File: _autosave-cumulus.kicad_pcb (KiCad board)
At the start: 2 copper layers, 147.6 x 122.3 mm, 42 parts

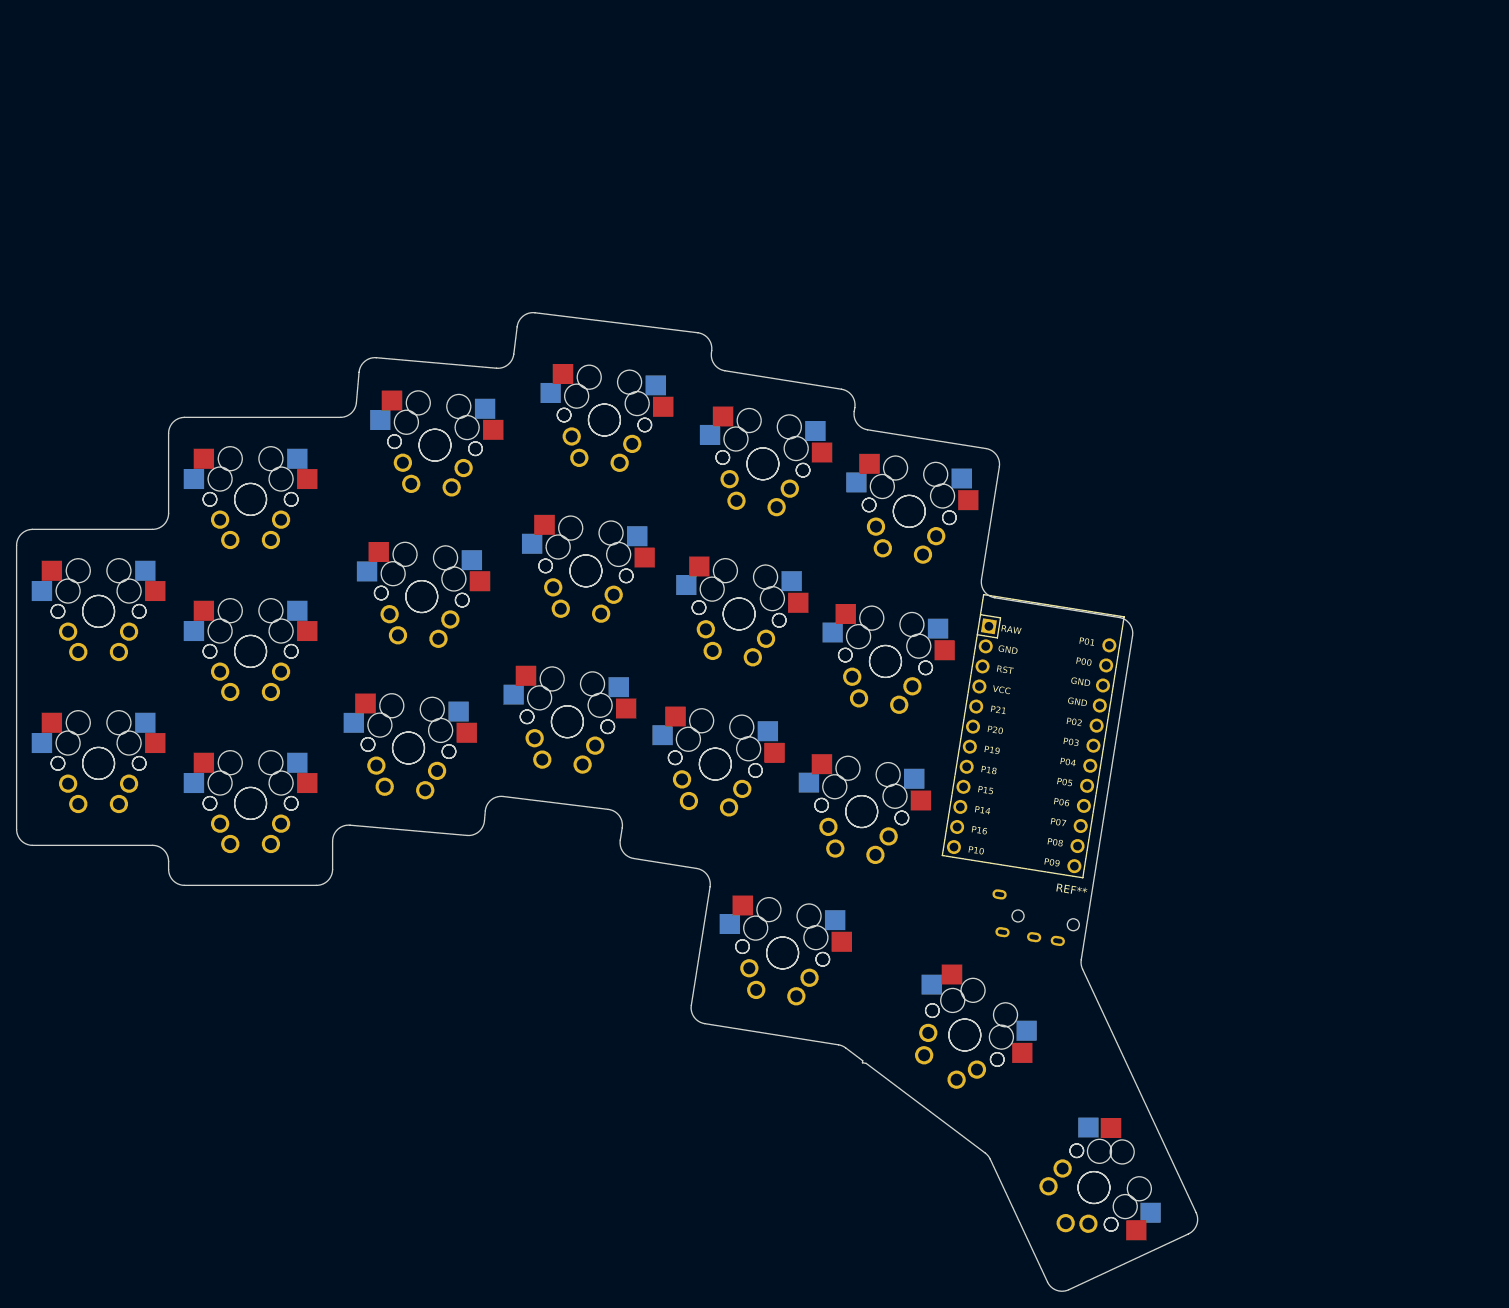
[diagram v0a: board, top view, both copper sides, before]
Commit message: Reversible ProMicro footprint added
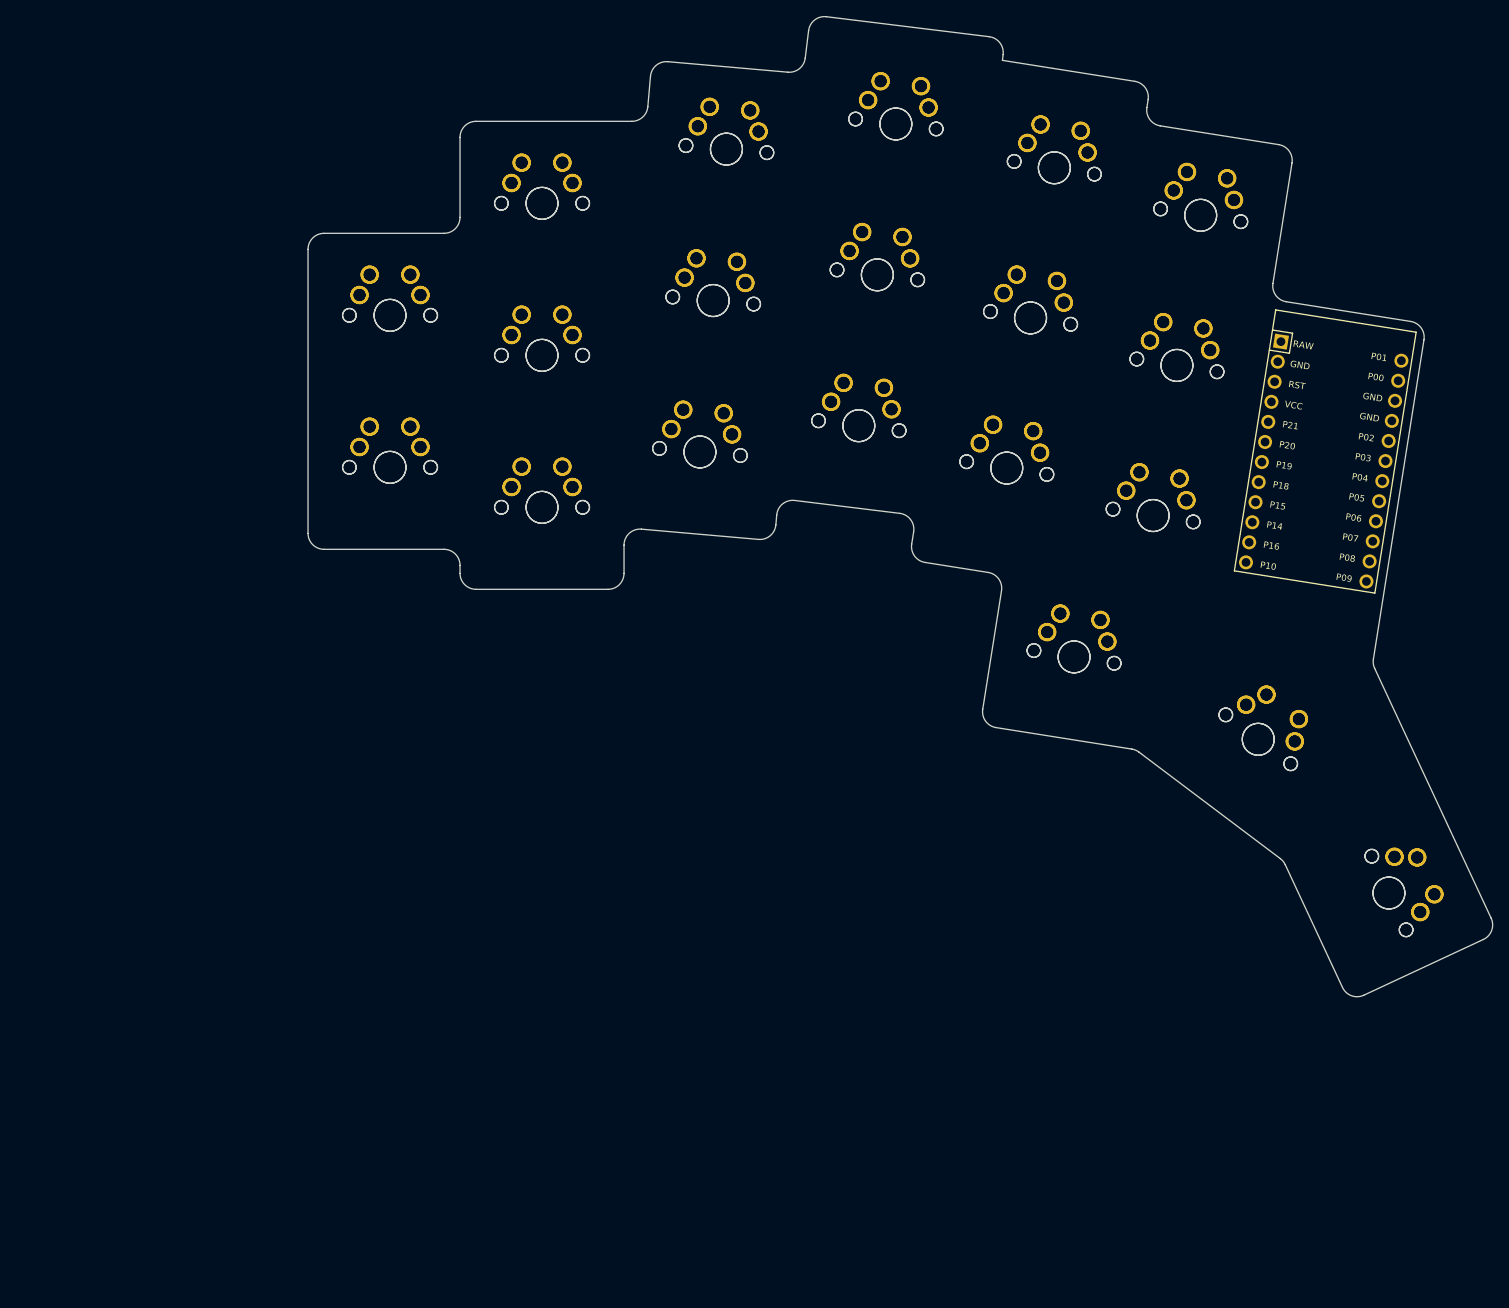
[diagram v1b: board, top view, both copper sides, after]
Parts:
- removed REF**: PJ-3200B-4A-Assembly, random-keyboard-parts:PJ-3200B-4A-Assembly
- moved S35 52.1 mm to (280.5, 194.6)
- moved S36 52.1 mm to (280.5, 194.6), turned to -65 degrees
- moved S33 52.1 mm to (264.2, 175.4)
- moved S34 52.1 mm to (264.2, 175.4), turned to -37 degrees
- moved S1 51.9 mm to (174.7, 146.4)
- moved S17 51.9 mm to (218.9, 98.5)
- moved S18 51.9 mm to (218.9, 98.5), turned to -7 degrees
- moved S19 51.9 mm to (232.8, 141.5)
- moved S2 51.9 mm to (174.7, 146.4), turned to 0 degrees
- moved S20 51.9 mm to (232.8, 141.5), turned to -9 degrees
- moved S21 51.9 mm to (235.7, 122.7)
- moved S22 51.9 mm to (235.7, 122.7), turned to -9 degrees
- moved S27 51.9 mm to (254.0, 128.7)
- moved S28 51.9 mm to (254.0, 128.7), turned to -9 degrees
- moved S31 51.9 mm to (241.2, 165.1)
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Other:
- board size 147.6 x 122.3 mm -> 148.1 x 122.5 mm
